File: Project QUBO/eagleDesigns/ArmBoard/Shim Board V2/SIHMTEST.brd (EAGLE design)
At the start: 71.1 x 81.3 mm, 30 parts, among them IC1 MCP2551/SN, U1 BME280

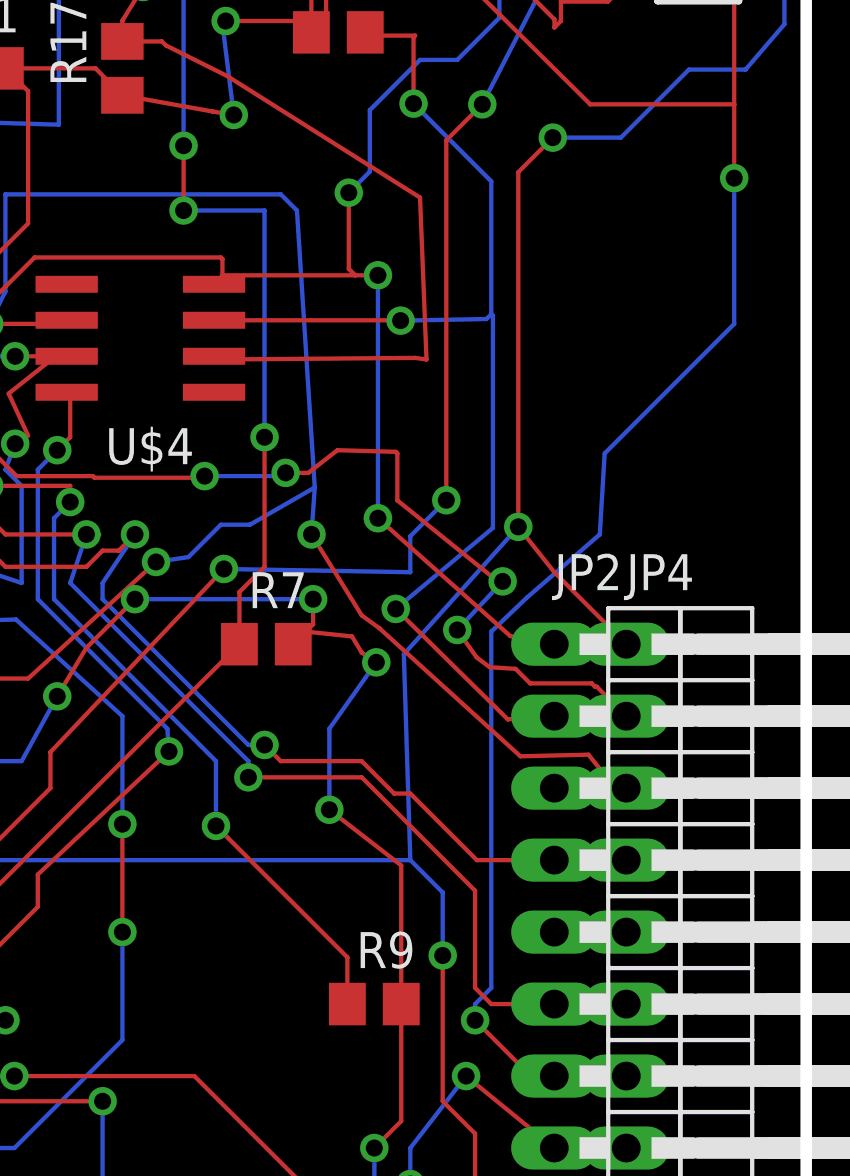
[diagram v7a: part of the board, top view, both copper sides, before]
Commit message: 
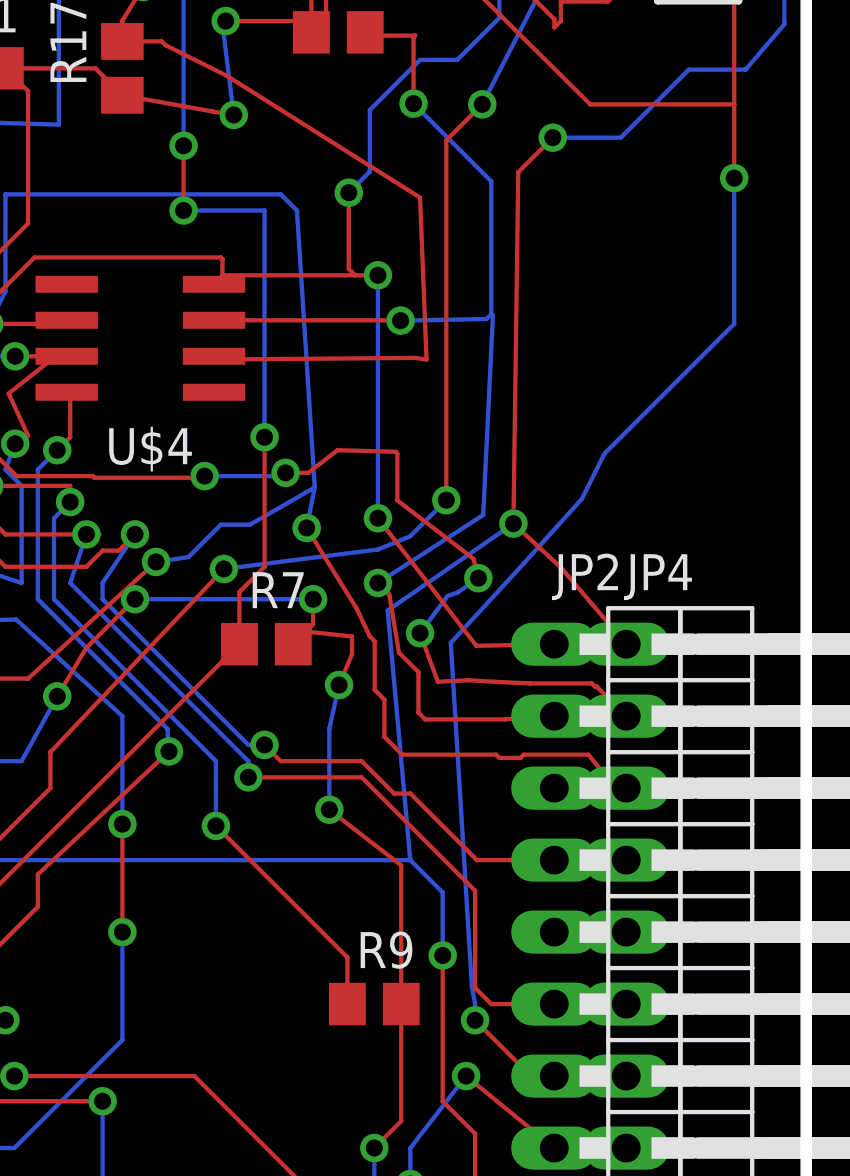
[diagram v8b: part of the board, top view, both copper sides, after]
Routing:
- net UNBUFFERSDA3: track 72.0 -> 74.3 mm
- net UNBUFFERSCL3: track 41.9 -> 44.1 mm
- net CANTX: track 50.9 -> 52.5 mm
- net 3.3(1): track 130.3 -> 129.2 mm
- net SPI_CLK: track 162.7 -> 163.7 mm
- net 5.0(BME): track 276.3 -> 275.5 mm
- net GND: track 315.3 -> 315.9 mm
